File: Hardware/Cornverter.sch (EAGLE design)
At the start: 156 parts, among them IC1 LD1117S50TR, IC2 MCP4822-E_SN, IC3 TL074D, IC4 TL074D, IC5 4050D, IC6 4050D, J1 MIDI_IN (Stereo TRS), J10 Ch2 Gate Out, J11 Ch2 Trig Out, J12 Clock Out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

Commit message: added the changes from spice sims to the schematic
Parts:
- added C27, C28: 100nF, rcl:C-EUC1206
- added IC7, IC8: 4050D, 40xx:4050D
- C22, C23: value 1nF -> 33nF
- R11, R6: value 22K -> 18K
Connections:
- new net N$116: IC8B.O, R38.2
- new net N$117: IC8C.O, R39.2
- new net N$118: IC8D.O, R40.2
- new net N$119: IC7A.O, JP9.1
- new net N$120: IC7B.O, JP9.2
- new net N$121: IC7C.O, JP11.1
- new net N$122: IC7D.O, JP11.2
- new net N$89: IC8A.O, R37.2
- net +5V: now also C27.1, C28.1, IC7P.VDD, IC8P.VDD
- net AGND: now also C27.2, C28.2, IC7P.VSS, IC8P.VSS
- net CH_1_ANA_1: now also IC7A.I; no longer JP9.1
- net CH_1_ANA_2: now also IC7B.I; no longer JP9.2
- net CH_2_ANA_1: now also IC7C.I; no longer JP11.1
- net CH_2_ANA_2: now also IC7D.I; no longer JP11.2
- net N$30: now also IC8D.I; no longer R40.2
- net N$34: now also IC8C.I; no longer R39.2
- net N$40: now also IC8B.I; no longer R38.2
- net N$44: now also IC8A.I; no longer R37.2
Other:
- moved on the sheet: C20, C21, LED10, LED11, LED12, LED9, R37, R38, R39, R40

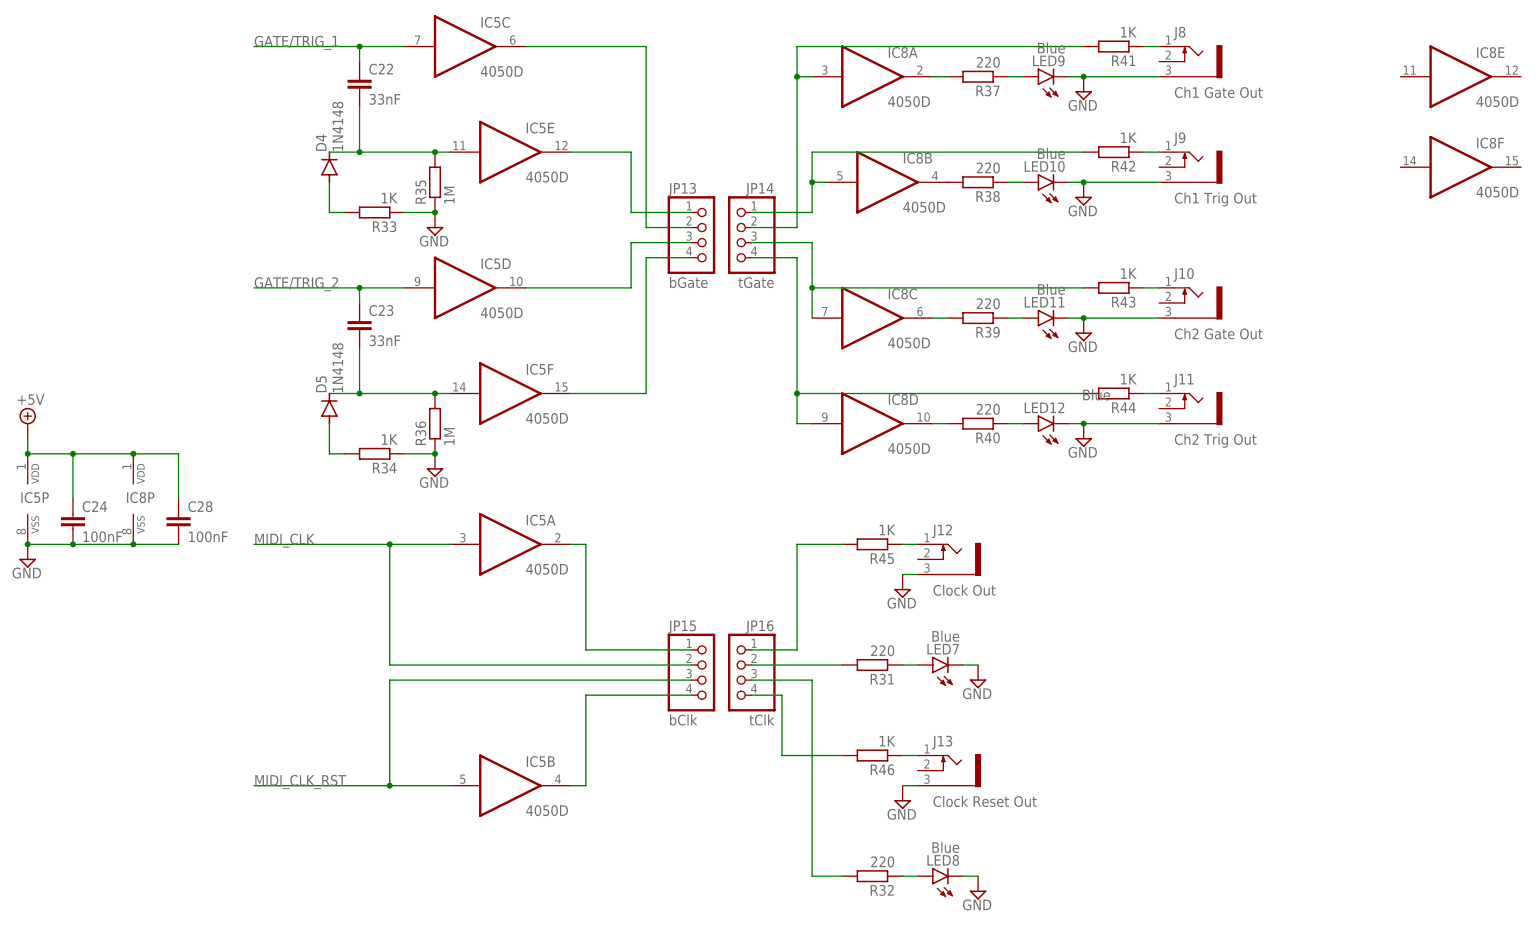
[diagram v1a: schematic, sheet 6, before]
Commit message: updated board design for the changes to schematic and ran ERC and DRC
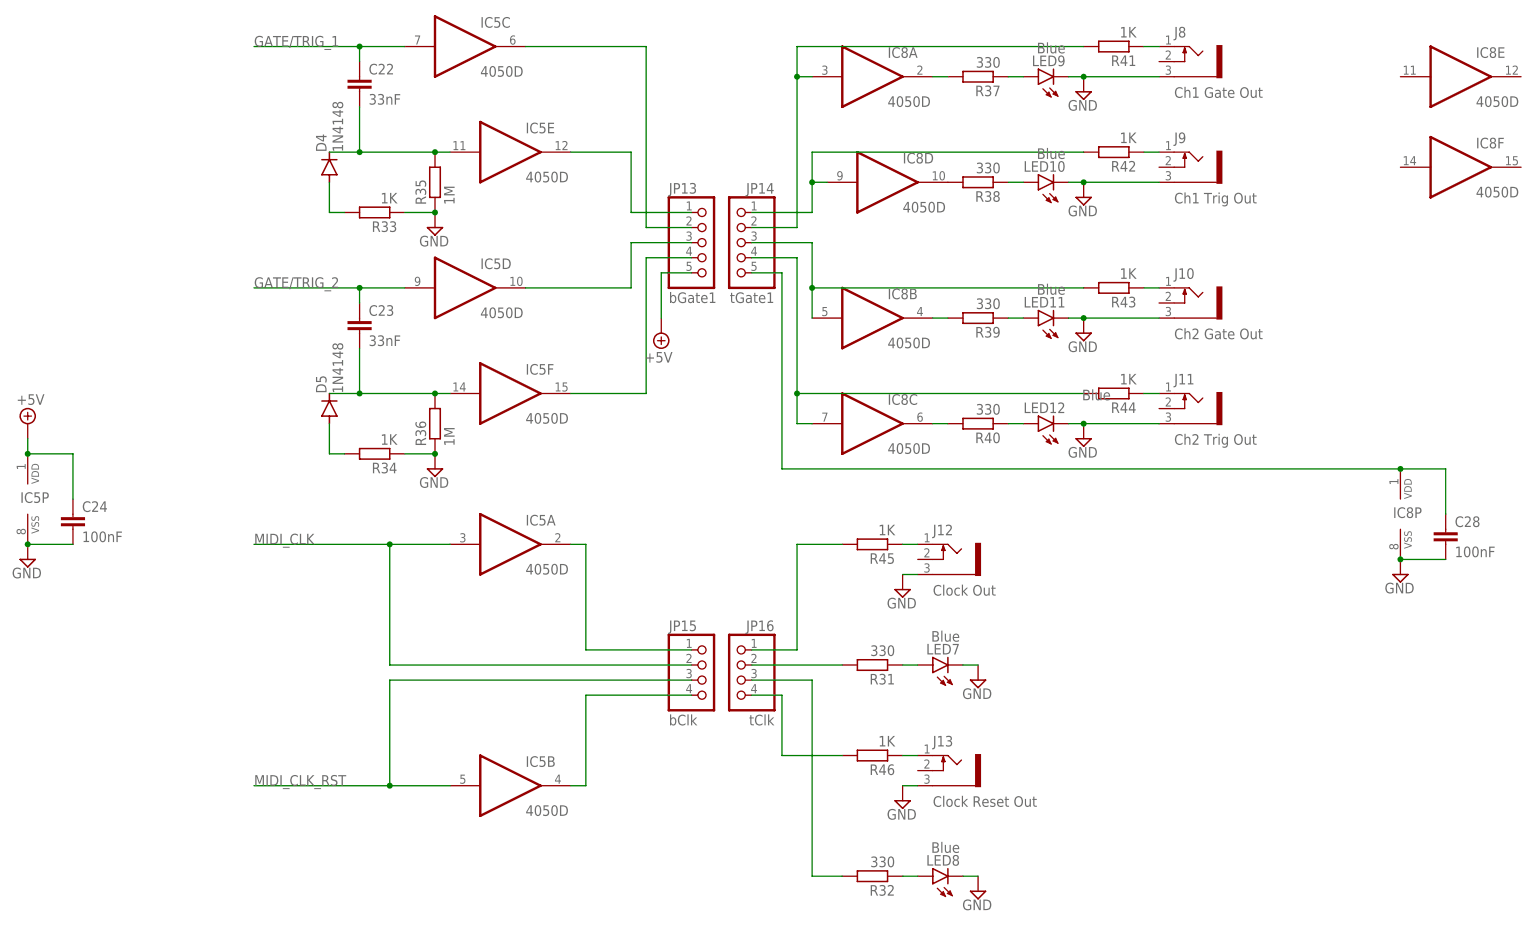
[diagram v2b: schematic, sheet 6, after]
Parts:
- JP13: value bGate -> bGate1; device pinhead:PINHD-1X4 -> pinhead:PINHD-1X5
- JP14: value tGate -> tGate1; device pinhead:PINHD-1X4 -> pinhead:PINHD-1X5
- R11, R6: value 18K -> 100K
- R13, R8: value 100K -> 105K
- R14, R9: value 220 -> 1K
- R15, R16, R17, R18, R31, R32, R37, R38, R39, R40, R47, R48, R49, R50, R51, R52: value 220 -> 330
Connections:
- new net TOP+5V: C28.1, IC8P.VDD, JP14.5
- net +5V: now also JP13.5; no longer C28.1, IC8P.VDD
- net N$116: now also IC8D.O; no longer IC8B.O
- net N$117: now also IC8B.O; no longer IC8C.O
- net N$118: now also IC8C.O; no longer IC8D.O
- net N$30: now also IC8C.I; no longer IC8D.I
- net N$34: now also IC8B.I; no longer IC8C.I
- net N$40: now also IC8D.I; no longer IC8B.I
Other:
- moved on the sheet: C28, IC8B, IC8C, IC8D, IC8P

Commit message: Added BOM, about to check all components
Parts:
- IC3, IC4: device linear:TL074D -> Improved parts:TL074D
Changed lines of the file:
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@@
 <attribute name="SPICEPREFIX" value="X"/>
 </part>
-<part name="IC4" library="linear" library_urn="urn:adsk.eagle:library:262" deviceset="TL074" device="D" package3d_urn="urn:adsk.eagle:package:16406/2" value="TL074D"/>
+<part name="IC4" library="Improved parts" deviceset="TL074" device="D" package3d_urn="urn:adsk.eagle:package:16406/2" value="TL074D"/>
 <part name="J2" library="thonkiconn" deviceset="WQP-PJ301M-12_JACK" device="" value="Ch1 Pitch Out"/>
 <part name="J3" library="thonkiconn" deviceset="WQP-PJ301M-12_JACK" device="" value="Ch2 Pitch Out"/>
@@
 <part name="R41" library="rcl" library_urn="urn:adsk.eagle:library:334" deviceset="R-EU_" device="R1206" package3d_urn="urn:adsk.eagle:package:23540/2" value="1K"/>
 <part name="R42" library="rcl" library_urn="urn:adsk.eagle:library:334" deviceset="R-EU_" device="R1206" package3d_urn="urn:adsk.eagle:package:23540/2" value="1K"/>
-<part name="IC3" library="linear" library_urn="urn:adsk.eagle:library:262" deviceset="TL074" device="D" package3d_urn="urn:adsk.eagle:package:16406/2" value="TL074D"/>
+<part name="IC3" library="Improved parts" deviceset="TL074" device="D" package3d_urn="urn:adsk.eagle:package:16406/2" value="TL074D"/>
 <part name="JP1" library="pinhead" library_urn="urn:adsk.eagle:library:325" deviceset="PINHD-2X3" device="" package3d_urn="urn:adsk.eagle:package:22462/2" value="ICSP"/>
 <part name="SUPPLY5" library="supply2" library_urn="urn:adsk.eagle:library:372" deviceset="AGND" device="" value="GND"/>

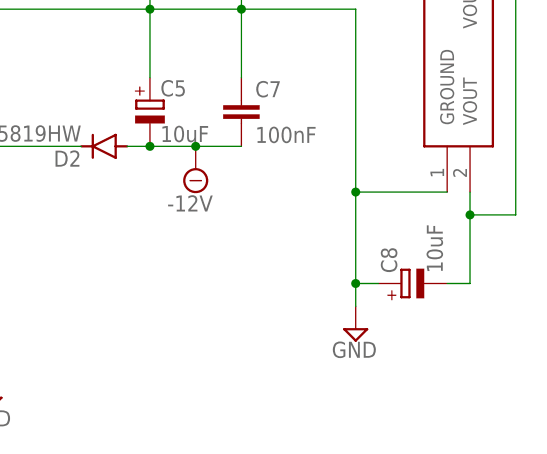
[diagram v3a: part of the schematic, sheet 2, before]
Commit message: Changed +5V 10uF electrolytic's polarity to be correct
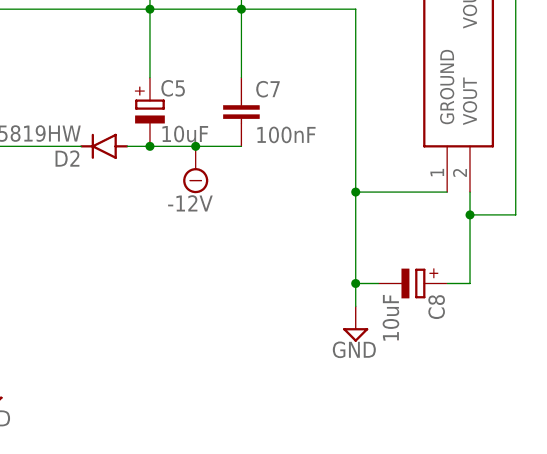
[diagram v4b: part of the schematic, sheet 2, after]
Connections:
- net +5V: now also C8.+; no longer C8.-
- net AGND: now also C8.-; no longer C8.+
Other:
- moved on the sheet: C8
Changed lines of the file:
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@@
 <attribute name="VALUE" x="59.944" y="30.861" size="1.778" layer="96"/>
 </instance>
-<instance part="C8" gate="G$1" x="76.2" y="-7.62" smashed="yes" rot="R90">
-<attribute name="NAME" x="75.7174" y="-6.477" size="1.778" layer="95" rot="R90"/>
-<attribute name="VALUE" x="80.7974" y="-6.477" size="1.778" layer="96" rot="R90"/>
+<instance part="C8" gate="G$1" x="78.74" y="-7.62" smashed="yes" rot="R270">
+<attribute name="NAME" x="79.2226" y="-8.763" size="1.778" layer="95" rot="R270"/>
+<attribute name="VALUE" x="74.1426" y="-8.763" size="1.778" layer="96" rot="R270"/>
 </instance>
 <instance part="C5" gate="G$1" x="48.26" y="12.7" smashed="yes">
@@
 <wire x1="71.12" y1="22.86" x2="71.12" y2="2.54" width="0.1524" layer="91"/>
 <pinref part="SUPPLY8" gate="G$1" pin="AGND"/>
-<pinref part="C8" gate="G$1" pin="+"/>
 <wire x1="71.12" y1="2.54" x2="71.12" y2="-7.62" width="0.1524" layer="91"/>
+<pinref part="IC1" gate="G$1" pin="GROUND"/>
 <wire x1="71.12" y1="-7.62" x2="71.12" y2="-10.16" width="0.1524" layer="91"/>
-<wire x1="73.66" y1="-7.62" x2="71.12" y2="-7.62" width="0.1524" layer="91"/>
-<pinref part="IC1" gate="G$1" pin="GROUND"/>
 <wire x1="81.28" y1="2.54" x2="71.12" y2="2.54" width="0.1524" layer="91"/>
 <junction x="71.12" y="2.54"/>
+<label x="12.7" y="22.86" size="1.778" layer="95"/>
+<pinref part="C8" gate="G$1" pin="-"/>
+<wire x1="71.12" y1="-7.62" x2="73.66" y2="-7.62" width="0.1524" layer="91"/>
 <junction x="71.12" y="-7.62"/>
-<label x="12.7" y="22.86" size="1.778" layer="95"/>
 </segment>
 <segment>
@@
 <net name="+5V" class="0">
 <segment>
-<pinref part="C8" gate="G$1" pin="-"/>
 <pinref part="IC1" gate="G$1" pin="VOUT"/>
-<wire x1="81.28" y1="-7.62" x2="83.82" y2="-7.62" width="0.1524" layer="91"/>
 <wire x1="83.82" y1="-7.62" x2="83.82" y2="0" width="0.1524" layer="91"/>
 <wire x1="83.82" y1="0" x2="83.82" y2="2.54" width="0.1524" layer="91"/>
@@
 <junction x="83.82" y="0"/>
 <junction x="86.36" y="38.1"/>
+<pinref part="C8" gate="G$1" pin="+"/>
+<wire x1="81.28" y1="-7.62" x2="83.82" y2="-7.62" width="0.1524" layer="91"/>
 </segment>
 </net>

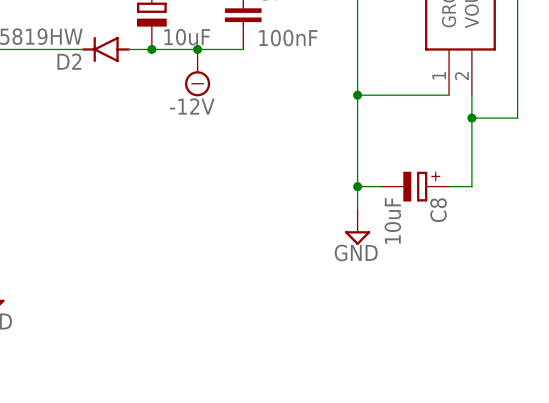
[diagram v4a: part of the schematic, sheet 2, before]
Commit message: Added 100nF bypass cap to 5V supply
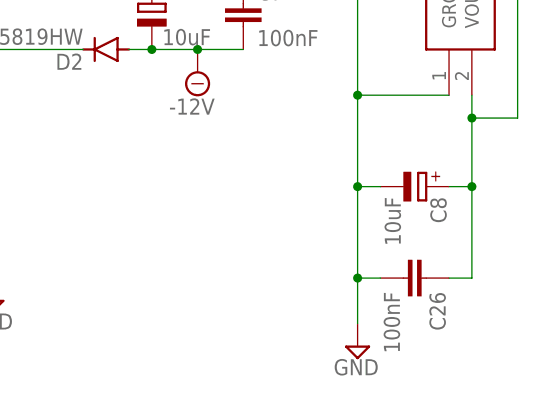
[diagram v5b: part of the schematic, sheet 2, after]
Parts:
- added C26: 100nF, rcl:C-EUC1206
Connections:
- net +5V: now also C26.1
- net AGND: now also C26.2
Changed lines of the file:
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@@
 <part name="SUPPLY71" library="supply2" library_urn="urn:adsk.eagle:library:372" deviceset="AGND" device="" value="GND"/>
 <part name="SUPPLY72" library="supply2" library_urn="urn:adsk.eagle:library:372" deviceset="+5V" device=""/>
+<part name="C26" library="rcl" library_urn="urn:adsk.eagle:library:334" deviceset="C-EU" device="C1206" package3d_urn="urn:adsk.eagle:package:23618/2" value="100nF"/>
 </parts>
 <sheets>
@@
 <attribute name="VALUE" x="84.455" y="43.815" size="1.778" layer="96"/>
 </instance>
-<instance part="SUPPLY8" gate="G$1" x="71.12" y="-12.7" smashed="yes">
-<attribute name="VALUE" x="68.453" y="-15.875" size="1.778" layer="96"/>
+<instance part="SUPPLY8" gate="G$1" x="71.12" y="-25.4" smashed="yes">
+<attribute name="VALUE" x="68.453" y="-28.575" size="1.778" layer="96"/>
 </instance>
 <instance part="IC1" gate="G$1" x="81.28" y="2.54" smashed="yes" rot="R90">
@@
 <attribute name="NAME" x="40.64" y="7.1374" size="1.778" layer="95" rot="R180"/>
 <attribute name="VALUE" x="40.64" y="9.9314" size="1.778" layer="96" rot="R180"/>
+</instance>
+<instance part="C26" gate="G$1" x="78.74" y="-17.78" smashed="yes" rot="R270">
+<attribute name="NAME" x="79.121" y="-19.304" size="1.778" layer="95" rot="R270"/>
+<attribute name="VALUE" x="74.041" y="-19.304" size="1.778" layer="96" rot="R270"/>
 </instance>
 </instances>
@@
 <wire x1="71.12" y1="2.54" x2="71.12" y2="-7.62" width="0.1524" layer="91"/>
 <pinref part="IC1" gate="G$1" pin="GROUND"/>
-<wire x1="71.12" y1="-7.62" x2="71.12" y2="-10.16" width="0.1524" layer="91"/>
+<wire x1="71.12" y1="-7.62" x2="71.12" y2="-17.78" width="0.1524" layer="91"/>
+<wire x1="71.12" y1="-17.78" x2="71.12" y2="-22.86" width="0.1524" layer="91"/>
 <wire x1="81.28" y1="2.54" x2="71.12" y2="2.54" width="0.1524" layer="91"/>
 <junction x="71.12" y="2.54"/>
@@
 <wire x1="71.12" y1="-7.62" x2="73.66" y2="-7.62" width="0.1524" layer="91"/>
 <junction x="71.12" y="-7.62"/>
+<pinref part="C26" gate="G$1" pin="2"/>
+<wire x1="73.66" y1="-17.78" x2="71.12" y2="-17.78" width="0.1524" layer="91"/>
+<junction x="71.12" y="-17.78"/>
 </segment>
 <segment>
@@
 <pinref part="C8" gate="G$1" pin="+"/>
 <wire x1="81.28" y1="-7.62" x2="83.82" y2="-7.62" width="0.1524" layer="91"/>
-</segment>
-</net>
+<pinref part="C26" gate="G$1" pin="1"/>
+<wire x1="81.28" y1="-17.78" x2="83.82" y2="-17.78" width="0.1524" layer="91"/>
+<wire x1="83.82" y1="-17.78" x2="83.82" y2="-7.62" width="0.1524" layer="91"/>
+<junction x="83.82" y="-7.62"/>
+</segment>
+</net>

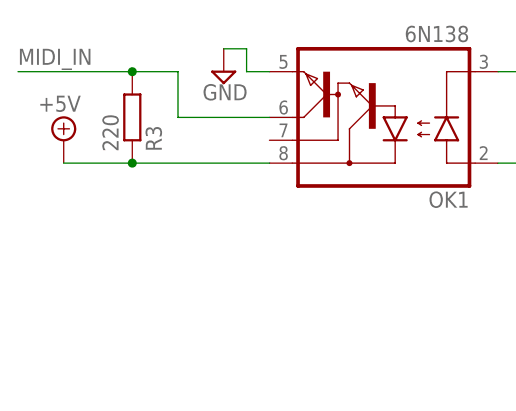
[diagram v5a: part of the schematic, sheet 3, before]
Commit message: Changed value of R3 (on the MCU side of the 6n138) from 220 to 280 ohms as per midi spec
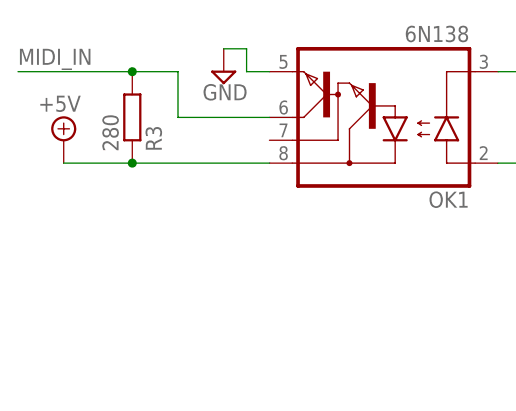
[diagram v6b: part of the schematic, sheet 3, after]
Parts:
- R3: value 220 -> 280
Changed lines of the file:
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@@
 <part name="R13" library="rcl" library_urn="urn:adsk.eagle:library:334" deviceset="R-EU_" device="R1206" package3d_urn="urn:adsk.eagle:package:23540/2" value="105K"/>
 <part name="R4" library="rcl" library_urn="urn:adsk.eagle:library:334" deviceset="R-EU_" device="R1206" package3d_urn="urn:adsk.eagle:package:23540/2" value="220"/>
-<part name="R3" library="rcl" library_urn="urn:adsk.eagle:library:334" deviceset="R-EU_" device="R1206" package3d_urn="urn:adsk.eagle:package:23540/2" value="220"/>
+<part name="R3" library="rcl" library_urn="urn:adsk.eagle:library:334" deviceset="R-EU_" device="R1206" package3d_urn="urn:adsk.eagle:package:23540/2" value="280"/>
 <part name="D3" library="diode" library_urn="urn:adsk.eagle:library:210" deviceset="1N4148" device="DO35-7" package3d_urn="urn:adsk.eagle:package:43339/1" value="1N4148"/>
 <part name="C22" library="rcl" library_urn="urn:adsk.eagle:library:334" deviceset="C-EU" device="C1206" package3d_urn="urn:adsk.eagle:package:23618/2" value="33nF"/>
